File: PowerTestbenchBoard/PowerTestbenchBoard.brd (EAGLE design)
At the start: 101.6 x 76.2 mm, 42 parts, among them J3 POWER_JACK, J5 POWER_JACK, J8 182-037-213R531, J9 182-025-213R531

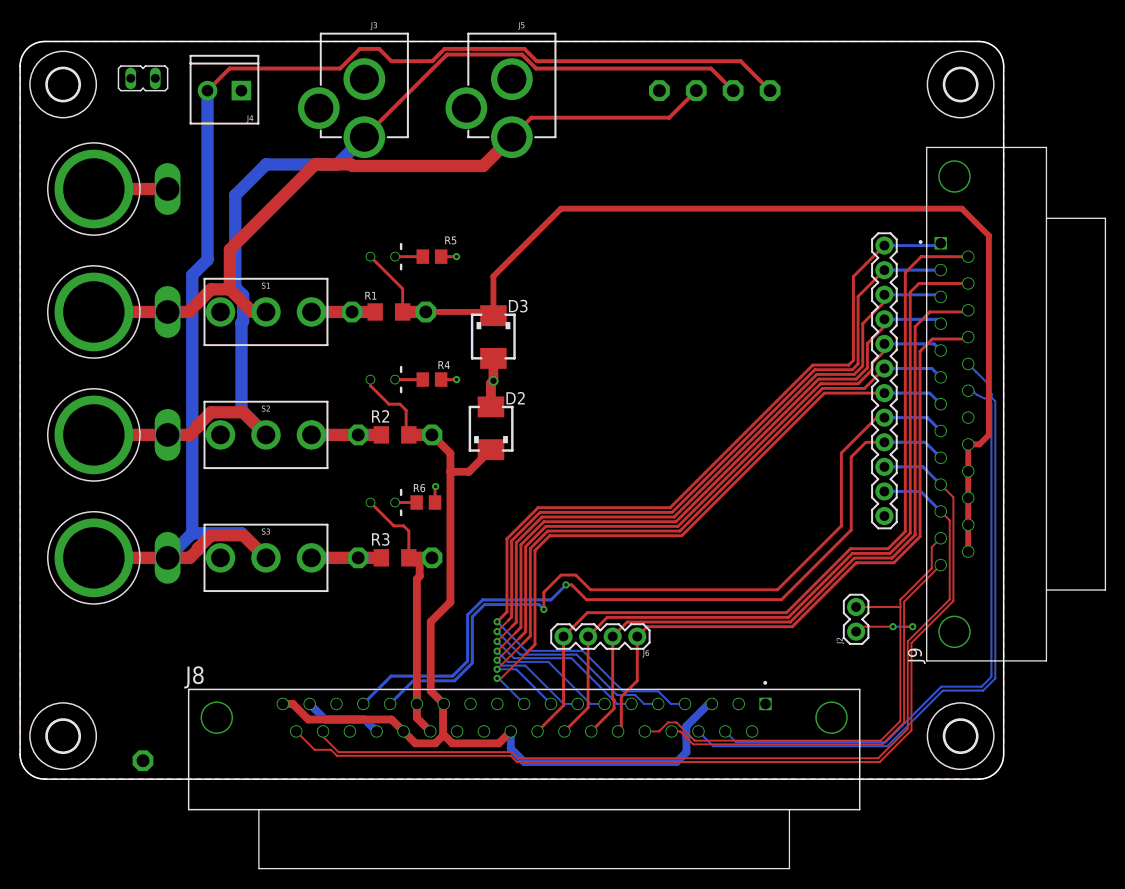
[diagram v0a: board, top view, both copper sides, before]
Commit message: Added caps on power busses. Enlarged power traces
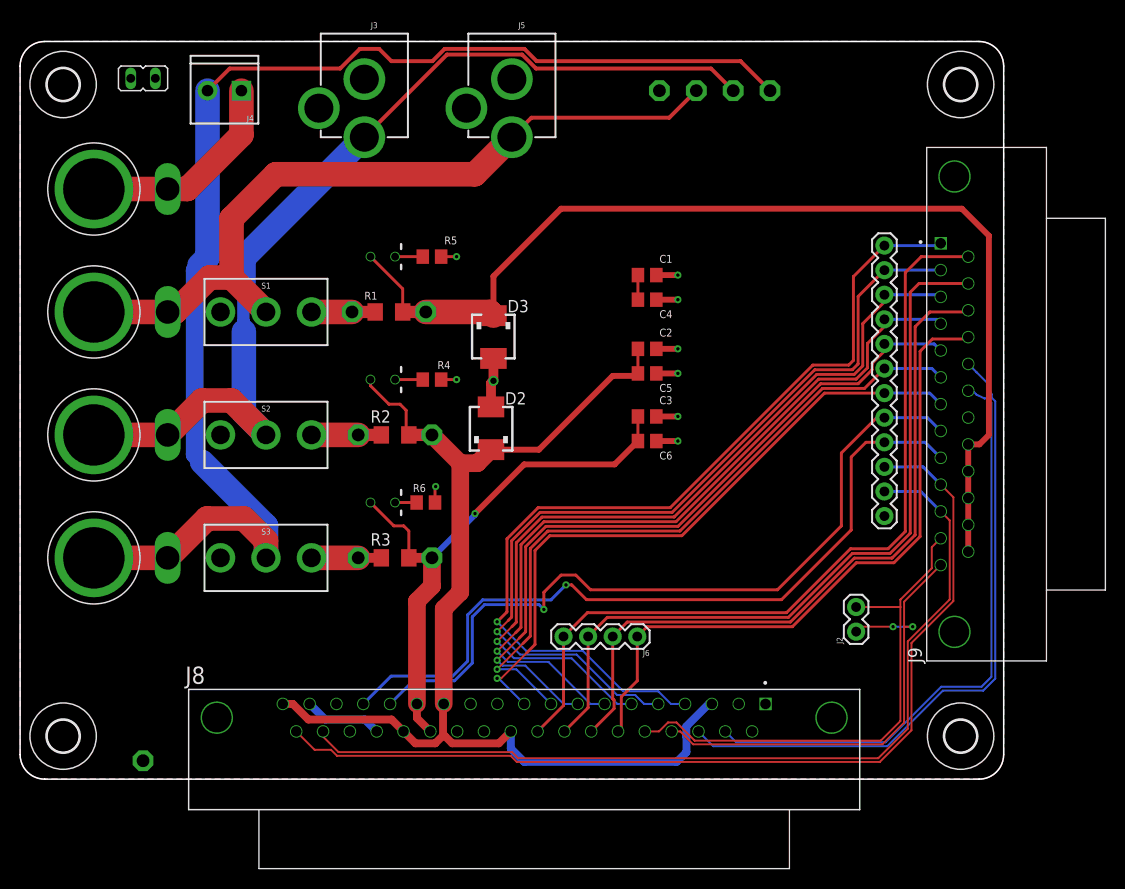
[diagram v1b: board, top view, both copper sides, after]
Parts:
- added C1, C2, C3: 0.1uF, rcl:C0805
- added C4, C5, C6: 10uF, rcl:C0805
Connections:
- net 12V: now also C3.1, C6.1
- net 5V-ACT: now also C2.1, C5.1
- net 5V-DIG: now also C1.1, C4.1
- net GND: now also C1.2, C2.2, C3.2, C4.2, C5.2, C6.2
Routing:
- net 12V: track 29.0 -> 58.4 mm, vias 0 -> 1
- net GND: track 17.6 -> 45.4 mm, vias 4 -> 10
- net 5V-ACT: track 102.4 -> 121.7 mm
- net 12V-IN: track 141.2 -> 136.8 mm
- net 5V-ACT-IN: track 105.0 -> 100.8 mm
- net 5V-DIG: track 118.2 -> 120.8 mm
- net 5V-DIG-IN: track 78.9 -> 80.3 mm

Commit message: Added jumper
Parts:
- added JP1: (no value), jumper:JP1
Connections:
- net 5V-ACT-IN: now also JP1.1
- net 5V-DIG-IN: now also JP1.2
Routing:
- net 5V-ACT-IN: track 100.8 -> 132.0 mm
- net 5V-DIG-IN: track 80.3 -> 89.2 mm
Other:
- board text added: "Jumper On- Connect 5V-Dig & 5V-Act inputs"
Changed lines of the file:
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@@
 Mark Gilliland, Graham Braly</text>
 <text x="54.61" y="31.75" size="1.6764" layer="51" rot="R180" align="center-right">Rev 1.0</text>
+<text x="60.452" y="75.692" size="0.8128" layer="51" rot="R90" align="center-right">Jumper On-
+Connect 5V-Dig
+&amp; 5V-Act inputs</text>
 </plain>
 <attributes>
@@
 <attribute name="VALUE" x="62.865" y="33.02" size="0.8128" layer="27"/>
 </element>
+<element name="JP1" library="jumper" library_urn="urn:adsk.eagle:library:252" package="JP1" package3d_urn="urn:adsk.eagle:package:15455/1" value="" x="60.96" y="66.04" smashed="yes" rot="R90">
+<attribute name="NAME" x="63.5" y="64.389" size="1.27" layer="25" ratio="10" rot="R180"/>
+<attribute name="VALUE" x="63.5" y="68.961" size="1.27" layer="27" ratio="10" rot="R180"/>
+</element>
 </elements>
 <signals>
@@
 <contactref element="S1" pad="2"/>
 <contactref element="TP2" pad="TP"/>
-<wire x1="50.8" y1="66.31" x2="52.816" y2="68.326" width="0.4064" layer="1"/>
+<wire x1="50.8" y1="66.31" x2="50.919" y2="66.429" width="0.4064" layer="1"/>
+<wire x1="50.919" y1="66.429" x2="52.816" y2="68.326" width="0.4064" layer="1"/>
 <wire x1="52.816" y1="68.326" x2="67.056" y2="68.326" width="0.4064" layer="1"/>
 <wire x1="67.056" y1="68.326" x2="69.85" y2="71.12" width="0.4064" layer="1"/>
@@
 <wire x1="21.844" y1="57.912" x2="21.844" y2="51.816" width="2.54" layer="1"/>
 <wire x1="46.974" y1="62.484" x2="26.416" y2="62.484" width="2.54" layer="1"/>
+<contactref element="JP1" pad="2"/>
+<wire x1="59.69" y1="66.04" x2="51.308" y2="66.04" width="2.54" layer="1"/>
+<wire x1="51.308" y1="66.04" x2="50.919" y2="66.429" width="2.54" layer="1"/>
 </signal>
 <signal name="5V-ACT-IN">
@@
 <wire x1="23.0632" y1="50.6984" x2="23.0632" y2="53.8132" width="2.54" layer="16"/>
 <wire x1="23.0632" y1="53.8132" x2="35.56" y2="66.31" width="2.54" layer="16"/>
+<contactref element="JP1" pad="1"/>
+<wire x1="35.56" y1="66.31" x2="39.862" y2="66.31" width="2.54" layer="16"/>
+<wire x1="39.862" y1="66.31" x2="43.688" y2="62.484" width="2.54" layer="16"/>
+<wire x1="62.23" y1="63.5" x2="62.23" y2="66.04" width="2.54" layer="16"/>
+<wire x1="43.688" y1="62.484" x2="61.214" y2="62.484" width="2.54" layer="16"/>
+<wire x1="61.214" y1="62.484" x2="62.23" y2="63.5" width="2.54" layer="16"/>
 </signal>
 <signal name="12V-IN">
